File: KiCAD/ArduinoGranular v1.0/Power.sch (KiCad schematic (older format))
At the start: 15 parts, among them J7 JST_BUS, J8 IDC_BUS, U1 TL072, U2 L7805, U3 TL074

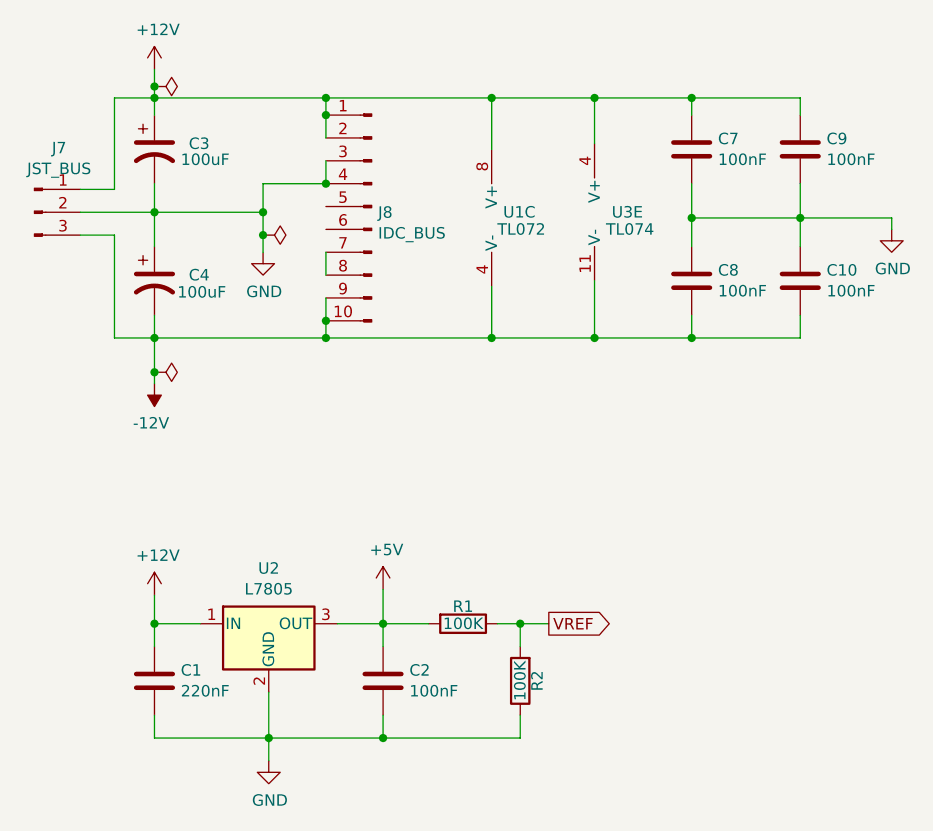
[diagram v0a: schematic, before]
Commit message: Marked NCs, fixed IDC bus grounds
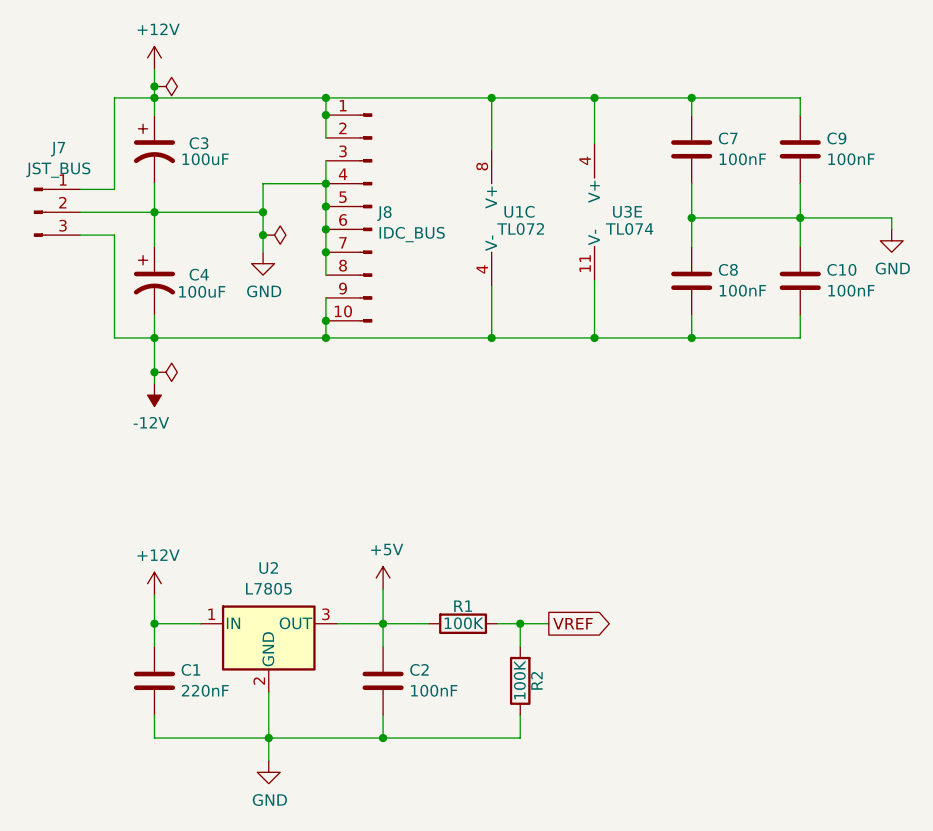
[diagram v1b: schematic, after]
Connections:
- net GND: now also J8.5 (Pin_5), J8.6 (Pin_6), J8.7 (Pin_7), J8.8 (Pin_8)
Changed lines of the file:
@@
 	1    0    0    -1
 $EndComp
+Wire Wire Line
+	5500 2525 5500 2625
+Connection ~ 5500 2825
+Connection ~ 5500 2625
+Wire Wire Line
+	5500 2625 5500 2725
+Connection ~ 5500 2725
+Wire Wire Line
+	5500 2725 5500 2825
 $EndSCHEMATC
